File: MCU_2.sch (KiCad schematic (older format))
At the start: 18 parts, among them U2 STM32F051K6Ux

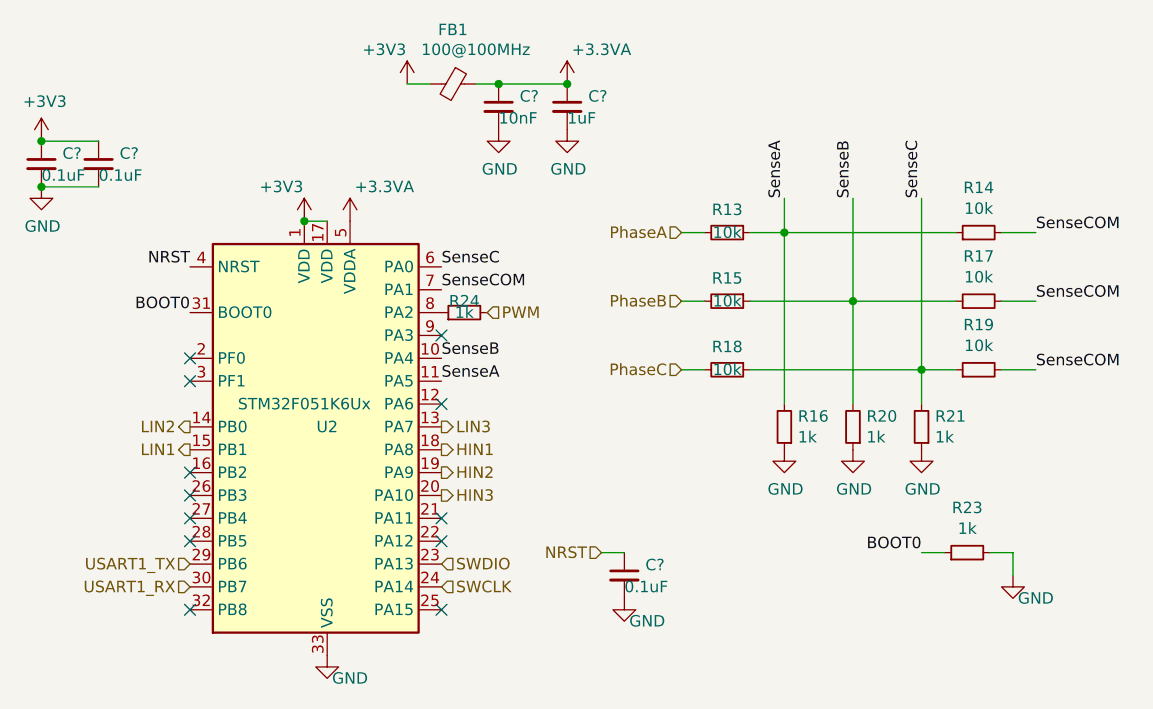
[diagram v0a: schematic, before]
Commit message: Added the rest of the phases and their associated components
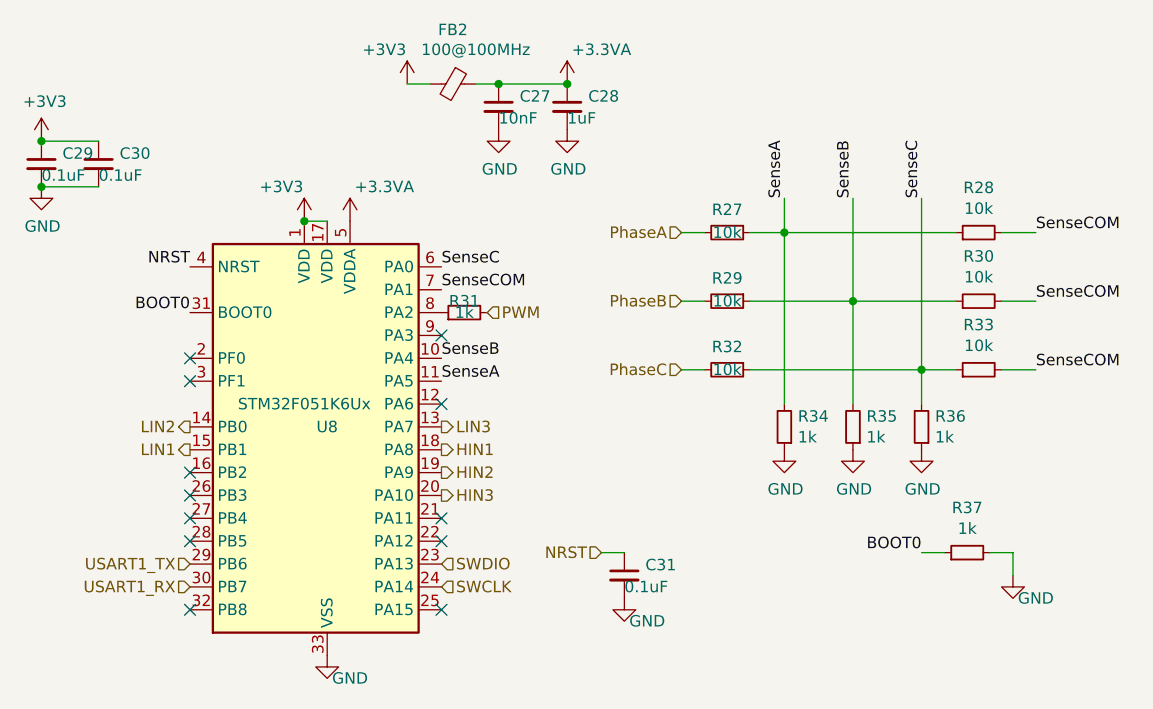
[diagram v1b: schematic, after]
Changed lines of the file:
@@
 $Descr A4 11693 8268
 encoding utf-8
-Sheet 7 7
+Sheet 6 11
 Title ""
 Date ""
@@
 AR Path="/605793E5/6059DC3A" Ref="U8"  Part="1"
 AR Path="/6057AB62/6059DC3A" Ref="U?"  Part="1"
-F 0 "U?" H 5050 2950 50  0000 C CNN
+F 0 "U8" H 5050 2950 50  0000 C CNN
 F 1 "STM32F051K6Ux" H 4950 3050 50  0000 C CNN
 F 2 "Package_DFN_QFN:QFN-32-1EP_5x5mm_P0.5mm_EP3.45x3.45mm" H 4550 2050 50  0001 R CNN
@@
 AR Path="/605793E5/6050F99C" Ref="#PWR0147"  Part="1"
 AR Path="/6057AB62/6050F99C" Ref="#PWR?"  Part="1"
-F 0 "#PWR?" H 4950 1900 50  0001 C CNN
+F 0 "#PWR0147" H 4950 1900 50  0001 C CNN
 F 1 "+3V3" H 4850 2200 50  0000 C CNN
 F 2 "" H 4950 2050 50  0001 C CNN
@@
 AR Path="/605793E5/6059DC2B" Ref="#PWR0148"  Part="1"
 AR Path="/6057AB62/6059DC2B" Ref="#PWR?"  Part="1"
-F 0 "#PWR?" H 5050 3700 50  0001 C CNN
+F 0 "#PWR0148" H 5050 3700 50  0001 C CNN
 F 1 "GND" H 5150 3850 50  0000 C CNN
 F 2 "" H 5050 3950 50  0001 C CNN
@@
 AR Path="/605793E5/6050F99E" Ref="C29"  Part="1"
 AR Path="/6057AB62/6050F99E" Ref="C?"  Part="1"
-F 0 "C?" H 3892 1846 50  0000 L CNN
+F 0 "C29" H 3892 1846 50  0000 L CNN
 F 1 "0.1uF" H 3800 1750 50  0000 L CNN
 F 2 "Capacitor_SMD:C_0402_1005Metric" H 3800 1800 50  0001 C CNN
@@
 AR Path="/605793E5/6059DC2C" Ref="#PWR0149"  Part="1"
 AR Path="/6057AB62/6059DC2C" Ref="#PWR?"  Part="1"
-F 0 "#PWR?" H 3800 1550 50  0001 C CNN
+F 0 "#PWR0149" H 3800 1550 50  0001 C CNN
 F 1 "+3V3" H 3815 1873 50  0000 C CNN
 F 2 "" H 3800 1700 50  0001 C CNN
@@
 AR Path="/605793E5/6059DC2D" Ref="#PWR0150"  Part="1"
 AR Path="/6057AB62/6059DC2D" Ref="#PWR?"  Part="1"
-F 0 "#PWR?" H 3800 1650 50  0001 C CNN
+F 0 "#PWR0150" H 3800 1650 50  0001 C CNN
 F 1 "GND" H 3805 1727 50  0000 C CNN
 F 2 "" H 3800 1900 50  0001 C CNN
@@
 AR Path="/605793E5/6059DC2E" Ref="C27"  Part="1"
 AR Path="/6057AB62/6059DC2E" Ref="C?"  Part="1"
-F 0 "C?" H 5892 1596 50  0000 L CNN
+F 0 "C27" H 5892 1596 50  0000 L CNN
 F 1 "10nF" H 5800 1500 50  0000 L CNN
 F 2 "Capacitor_SMD:C_0402_1005Metric" H 5800 1550 50  0001 C CNN
@@
 AR Path="/605793E5/6059DC2F" Ref="C30"  Part="1"
 AR Path="/6057AB62/6059DC2F" Ref="C?"  Part="1"
-F 0 "C?" H 4142 1846 50  0000 L CNN
+F 0 "C30" H 4142 1846 50  0000 L CNN
 F 1 "0.1uF" H 4050 1750 50  0000 L CNN
 F 2 "Capacitor_SMD:C_0402_1005Metric" H 4050 1800 50  0001 C CNN
@@
 AR Path="/605793E5/60384B76" Ref="R34"  Part="1"
 AR Path="/6057AB62/60384B76" Ref="R?"  Part="1"
-F 0 "R?" H 6991 2904 50  0000 R CNN
+F 0 "R34" H 6991 2904 50  0000 R CNN
 F 1 "1k" H 6991 2995 50  0000 R CNN
 F 2 "Resistor_SMD:R_0402_1005Metric" H 7050 2950 50  0001 C CNN
@@
 AR Path="/605793E5/6038543F" Ref="#PWR0151"  Part="1"
 AR Path="/6057AB62/6038543F" Ref="#PWR?"  Part="1"
-F 0 "#PWR?" H 7050 2800 50  0001 C CNN
+F 0 "#PWR0151" H 7050 2800 50  0001 C CNN
 F 1 "GND" H 7055 2877 50  0000 C CNN
 F 2 "" H 7050 3050 50  0001 C CNN
@@
 AR Path="/605793E5/60383909" Ref="R27"  Part="1"
 AR Path="/6057AB62/60383909" Ref="R?"  Part="1"
-F 0 "R?" V 6700 2100 50  0000 C CNN
+F 0 "R27" V 6700 2100 50  0000 C CNN
 F 1 "10k" V 6800 2100 50  0000 C CNN
 F 2 "Resistor_SMD:R_0402_1005Metric" H 6800 2100 50  0001 C CNN
@@
 AR Path="/605793E5/60386A06" Ref="R28"  Part="1"
 AR Path="/6057AB62/60386A06" Ref="R?"  Part="1"
-F 0 "R?" V 8096 2100 50  0000 C CNN
+F 0 "R28" V 8096 2100 50  0000 C CNN
 F 1 "10k" V 8005 2100 50  0000 C CNN
 F 2 "Resistor_SMD:R_0402_1005Metric" H 7900 2100 50  0001 C CNN
@@
 AR Path="/605793E5/6059DC3D" Ref="R29"  Part="1"
 AR Path="/6057AB62/6059DC3D" Ref="R?"  Part="1"
-F 0 "R?" V 6700 2400 50  0000 C CNN
+F 0 "R29" V 6700 2400 50  0000 C CNN
 F 1 "10k" V 6800 2400 50  0000 C CNN
 F 2 "Resistor_SMD:R_0402_1005Metric" H 6800 2400 50  0001 C CNN
@@
 AR Path="/605793E5/6059DC3E" Ref="R32"  Part="1"
 AR Path="/6057AB62/6059DC3E" Ref="R?"  Part="1"
-F 0 "R?" V 6700 2700 50  0000 C CNN
+F 0 "R32" V 6700 2700 50  0000 C CNN
 F 1 "10k" V 6800 2700 50  0000 C CNN
 F 2 "Resistor_SMD:R_0402_1005Metric" H 6800 2700 50  0001 C CNN
@@
 AR Path="/605793E5/6050F9A9" Ref="R35"  Part="1"
 AR Path="/6057AB62/6050F9A9" Ref="R?"  Part="1"
-F 0 "R?" H 7291 2904 50  0000 R CNN
+F 0 "R35" H 7291 2904 50  0000 R CNN
 F 1 "1k" H 7291 2995 50  0000 R CNN
 F 2 "Resistor_SMD:R_0402_1005Metric" H 7350 2950 50  0001 C CNN
@@
 AR Path="/605793E5/6050F9AA" Ref="R36"  Part="1"
 AR Path="/6057AB62/6050F9AA" Ref="R?"  Part="1"
-F 0 "R?" H 7591 2904 50  0000 R CNN
+F 0 "R36" H 7591 2904 50  0000 R CNN
 F 1 "1k" H 7591 2995 50  0000 R CNN
 F 2 "Resistor_SMD:R_0402_1005Metric" H 7650 2950 50  0001 C CNN
@@
 AR Path="/605793E5/6050F9AB" Ref="R30"  Part="1"
 AR Path="/6057AB62/6050F9AB" Ref="R?"  Part="1"
-F 0 "R?" V 8096 2400 50  0000 C CNN
+F 0 "R30" V 8096 2400 50  0000 C CNN
 F 1 "10k" V 8005 2400 50  0000 C CNN
 F 2 "Resistor_SMD:R_0402_1005Metric" H 7900 2400 50  0001 C CNN
@@
 AR Path="/605793E5/6050F9AC" Ref="R33"  Part="1"
 AR Path="/6057AB62/6050F9AC" Ref="R?"  Part="1"
-F 0 "R?" V 8096 2700 50  0000 C CNN
+F 0 "R33" V 8096 2700 50  0000 C CNN
 F 1 "10k" V 8005 2700 50  0000 C CNN
 F 2 "Resistor_SMD:R_0402_1005Metric" H 7900 2700 50  0001 C CNN
@@
 AR Path="/605793E5/6050F9AD" Ref="#PWR0152"  Part="1"
 AR Path="/6057AB62/6050F9AD" Ref="#PWR?"  Part="1"
-F 0 "#PWR?" H 7350 2800 50  0001 C CNN
+F 0 "#PWR0152" H 7350 2800 50  0001 C CNN
 F 1 "GND" H 7355 2877 50  0000 C CNN
 F 2 "" H 7350 3050 50  0001 C CNN
@@
 AR Path="/605793E5/60397C4C" Ref="#PWR0153"  Part="1"
 AR Path="/6057AB62/60397C4C" Ref="#PWR?"  Part="1"
-F 0 "#PWR?" H 7650 2800 50  0001 C CNN
+F 0 "#PWR0153" H 7650 2800 50  0001 C CNN
 F 1 "GND" H 7655 2877 50  0000 C CNN
 F 2 "" H 7650 3050 50  0001 C CNN
@@
 AR Path="/605793E5/6059DC44" Ref="#PWR0154"  Part="1"
 AR Path="/6057AB62/6059DC44" Ref="#PWR?"  Part="1"
-F 0 "#PWR?" H 6350 3450 50  0001 C CNN
+F 0 "#PWR0154" H 6350 3450 50  0001 C CNN
 F 1 "GND" H 6450 3600 50  0000 C CNN
 F 2 "" H 6350 3700 50  0001 C CNN
@@
 AR Path="/605793E5/6059DC45" Ref="R37"  Part="1"
 AR Path="/6057AB62/6059DC45" Ref="R?"  Part="1"
-F 0 "R?" V 8046 3500 50  0000 C CNN
+F 0 "R37" V 8046 3500 50  0000 C CNN
 F 1 "1k" V 7955 3500 50  0000 C CNN
 F 2 "Resistor_SMD:R_0402_1005Metric" H 7850 3500 50  0001 C CNN
@@
 AR Path="/605793E5/6059DC46" Ref="#PWR0155"  Part="1"
 AR Path="/6057AB62/6059DC46" Ref="#PWR?"  Part="1"
-F 0 "#PWR?" H 8050 3350 50  0001 C CNN
+F 0 "#PWR0155" H 8050 3350 50  0001 C CNN
 F 1 "GND" H 8150 3500 50  0000 C CNN
 F 2 "" H 8050 3600 50  0001 C CNN
@@
 AR Path="/605793E5/6050F9B2" Ref="R31"  Part="1"
 AR Path="/6057AB62/6050F9B2" Ref="R?"  Part="1"
-F 0 "R?" V 5700 2450 50  0000 C CNN
+F 0 "R31" V 5700 2450 50  0000 C CNN
 F 1 "1k" V 5650 2450 50  0000 C CNN
 F 2 "Resistor_SMD:R_0402_1005Metric" H 5650 2450 50  0001 C CNN
@@
 AR Path="/605793E5/6050F9B3" Ref="C31"  Part="1"
 AR Path="/6057AB62/6050F9B3" Ref="C?"  Part="1"
-F 0 "C?" H 6442 3646 50  0000 L CNN
+F 0 "C31" H 6442 3646 50  0000 L CNN
 F 1 "0.1uF" H 6350 3550 50  0000 L CNN
 F 2 "Capacitor_SMD:C_0402_1005Metric" H 6350 3600 50  0001 C CNN
@@
 AR Path="/605793E5/6050F9B4" Ref="#PWR0156"  Part="1"
 AR Path="/6057AB62/6050F9B4" Ref="#PWR?"  Part="1"
-F 0 "#PWR?" H 5150 1900 50  0001 C CNN
+F 0 "#PWR0156" H 5150 1900 50  0001 C CNN
 F 1 "+3.3VA" H 5300 2200 50  0000 C CNN
 F 2 "" H 5150 2050 50  0001 C CNN
@@
 AR Path="/605793E5/6059DC35" Ref="#PWR0157"  Part="1"
 AR Path="/6057AB62/6059DC35" Ref="#PWR?"  Part="1"
-F 0 "#PWR?" H 5400 1300 50  0001 C CNN
+F 0 "#PWR0157" H 5400 1300 50  0001 C CNN
 F 1 "+3V3" H 5300 1600 50  0000 C CNN
 F 2 "" H 5400 1450 50  0001 C CNN
@@
 AR Path="/605793E5/604552DE" Ref="#PWR0158"  Part="1"
 AR Path="/6057AB62/604552DE" Ref="#PWR?"  Part="1"
-F 0 "#PWR?" H 6100 1300 50  0001 C CNN
+F 0 "#PWR0158" H 6100 1300 50  0001 C CNN
 F 1 "+3.3VA" H 6250 1600 50  0000 C CNN
 F 2 "" H 6100 1450 50  0001 C CNN
@@
 AR Path="/605793E5/604562F9" Ref="C28"  Part="1"
 AR Path="/6057AB62/604562F9" Ref="C?"  Part="1"
-F 0 "C?" H 6192 1596 50  0000 L CNN
+F 0 "C28" H 6192 1596 50  0000 L CNN
 F 1 "1uF" H 6100 1500 50  0000 L CNN
 F 2 "Capacitor_SMD:C_0402_1005Metric" H 6100 1550 50  0001 C CNN
@@
 AR Path="/605793E5/6045758B" Ref="FB2"  Part="1"
 AR Path="/6057AB62/6045758B" Ref="FB?"  Part="1"
-F 0 "FB?" V 5363 1450 50  0000 C CNN
+F 0 "FB2" V 5363 1450 50  0000 C CNN
 F 1 "100@100MHz" V 5450 1550 50  0000 C CNN
 F 2 "Inductor_SMD:L_0603_1608Metric" V 5530 1450 50  0001 C CNN
@@
 AR Path="/605793E5/6045A51B" Ref="#PWR0159"  Part="1"
 AR Path="/6057AB62/6045A51B" Ref="#PWR?"  Part="1"
-F 0 "#PWR?" H 6100 1400 50  0001 C CNN
+F 0 "#PWR0159" H 6100 1400 50  0001 C CNN
 F 1 "GND" H 6105 1477 50  0000 C CNN
 F 2 "" H 6100 1650 50  0001 C CNN
@@
 AR Path="/605793E5/6050F9BA" Ref="#PWR0160"  Part="1"
 AR Path="/6057AB62/6050F9BA" Ref="#PWR?"  Part="1"
-F 0 "#PWR?" H 5800 1400 50  0001 C CNN
+F 0 "#PWR0160" H 5800 1400 50  0001 C CNN
 F 1 "GND" H 5805 1477 50  0000 C CNN
 F 2 "" H 5800 1650 50  0001 C CNN

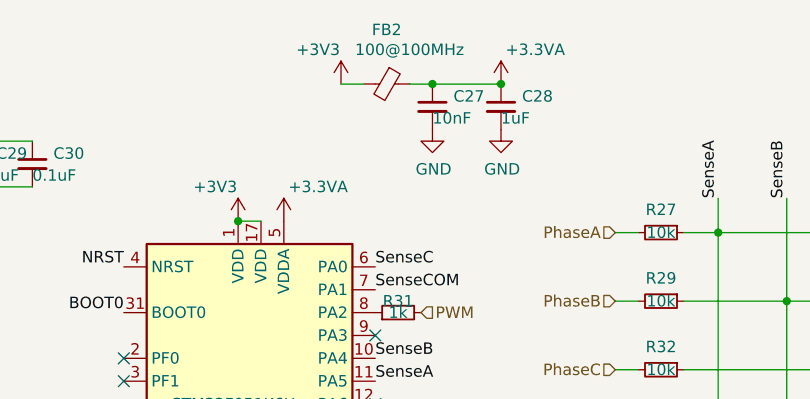
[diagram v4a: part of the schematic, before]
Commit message: Finished all traces and vias
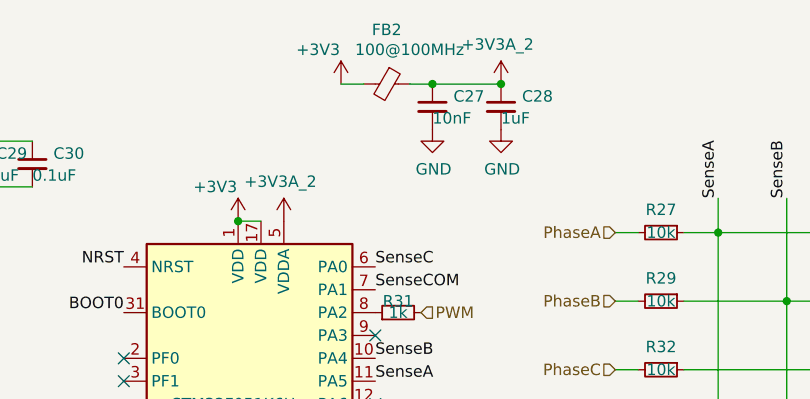
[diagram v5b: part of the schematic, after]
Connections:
- net +3.3VA renamed +3.3VA_2
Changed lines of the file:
@@
 NRST
-$Comp
-L power:+3.3VA #PWR0109
-U 1 1 6050F9B4
-P 5150 2050
-AR Path="/60302A40/6050F9B4" Ref="#PWR0109"  Part="1"
-AR Path="/605793E5/6050F9B4" Ref="#PWR0156"  Part="1"
-AR Path="/6057AB62/6050F9B4" Ref="#PWR?"  Part="1"
-AR Path="/6054D32F/6050F9B4" Ref="#PWR0127"  Part="1"
-AR Path="/60568CD3/6050F9B4" Ref="#PWR?"  Part="1"
-AR Path="/60575054/6050F9B4" Ref="#PWR?"  Part="1"
-AR Path="/60595215/6050F9B4" Ref="#PWR0189"  Part="1"
-AR Path="/605A2EB9/6050F9B4" Ref="#PWR0214"  Part="1"
-AR Path="/60535FFC/6050F9B4" Ref="#PWR0187"  Part="1"
-F 0 "#PWR0156" H 5150 1900 50  0001 C CNN
-F 1 "+3.3VA" H 5300 2200 50  0000 C CNN
-F 2 "" H 5150 2050 50  0001 C CNN
-F 3 "" H 5150 2050 50  0001 C CNN
-	1    5150 2050
-	1    0    0    -1
-$EndComp
 $Comp
 L power:+3V3 #PWR0110
@@
 F 3 "" H 5400 1450 50  0001 C CNN
 	1    5400 1450
-	1    0    0    -1
-$EndComp
-$Comp
-L power:+3.3VA #PWR0111
-U 1 1 604552DE
-P 6100 1450
-AR Path="/60302A40/604552DE" Ref="#PWR0111"  Part="1"
-AR Path="/605793E5/604552DE" Ref="#PWR0158"  Part="1"
-AR Path="/6057AB62/604552DE" Ref="#PWR?"  Part="1"
-AR Path="/6054D32F/604552DE" Ref="#PWR0162"  Part="1"
-AR Path="/60568CD3/604552DE" Ref="#PWR?"  Part="1"
-AR Path="/60575054/604552DE" Ref="#PWR?"  Part="1"
-AR Path="/60595215/604552DE" Ref="#PWR0191"  Part="1"
-AR Path="/605A2EB9/604552DE" Ref="#PWR0220"  Part="1"
-AR Path="/60535FFC/604552DE" Ref="#PWR0189"  Part="1"
-F 0 "#PWR0158" H 6100 1300 50  0001 C CNN
-F 1 "+3.3VA" H 6250 1600 50  0000 C CNN
-F 2 "" H 6100 1450 50  0001 C CNN
-F 3 "" H 6100 1450 50  0001 C CNN
-	1    6100 1450
 	1    0    0    -1
 $EndComp
@@
 Wire Wire Line
 	5700 1450 5800 1450
-Connection ~ 6100 1450
 Wire Wire Line
 	5800 1450 6100 1450
@@
 Text HLabel 4450 3550 0    50   Input ~ 0
 USART1_TX
+$Comp
+L power:+3V3A_2 #PWR0214
+U 1 1 605631A2
+P 5150 2050
+F 0 "#PWR0214" H 5150 2000 50  0001 C CNN
+F 1 "+3V3A_2" H 5135 2223 50  0000 C CNN
+F 2 "" H 5150 2050 50  0001 C CNN
+F 3 "" H 5150 2050 50  0001 C CNN
+	1    5150 2050
+	1    0    0    -1
+$EndComp
+$Comp
+L power:+3V3A_2 #PWR?
+U 1 1 6056D000
+P 6100 1450
+F 0 "#PWR?" H 6100 1400 50  0001 C CNN
+F 1 "+3V3A_2" H 6085 1623 50  0000 C CNN
+F 2 "" H 6100 1450 50  0001 C CNN
+F 3 "" H 6100 1450 50  0001 C CNN
+	1    6100 1450
+	1    0    0    -1
+$EndComp
+Connection ~ 6100 1450
 $EndSCHEMATC
